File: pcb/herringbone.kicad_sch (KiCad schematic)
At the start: 93 parts, among them U1 ATmega328P-PU, Y1 16MHz

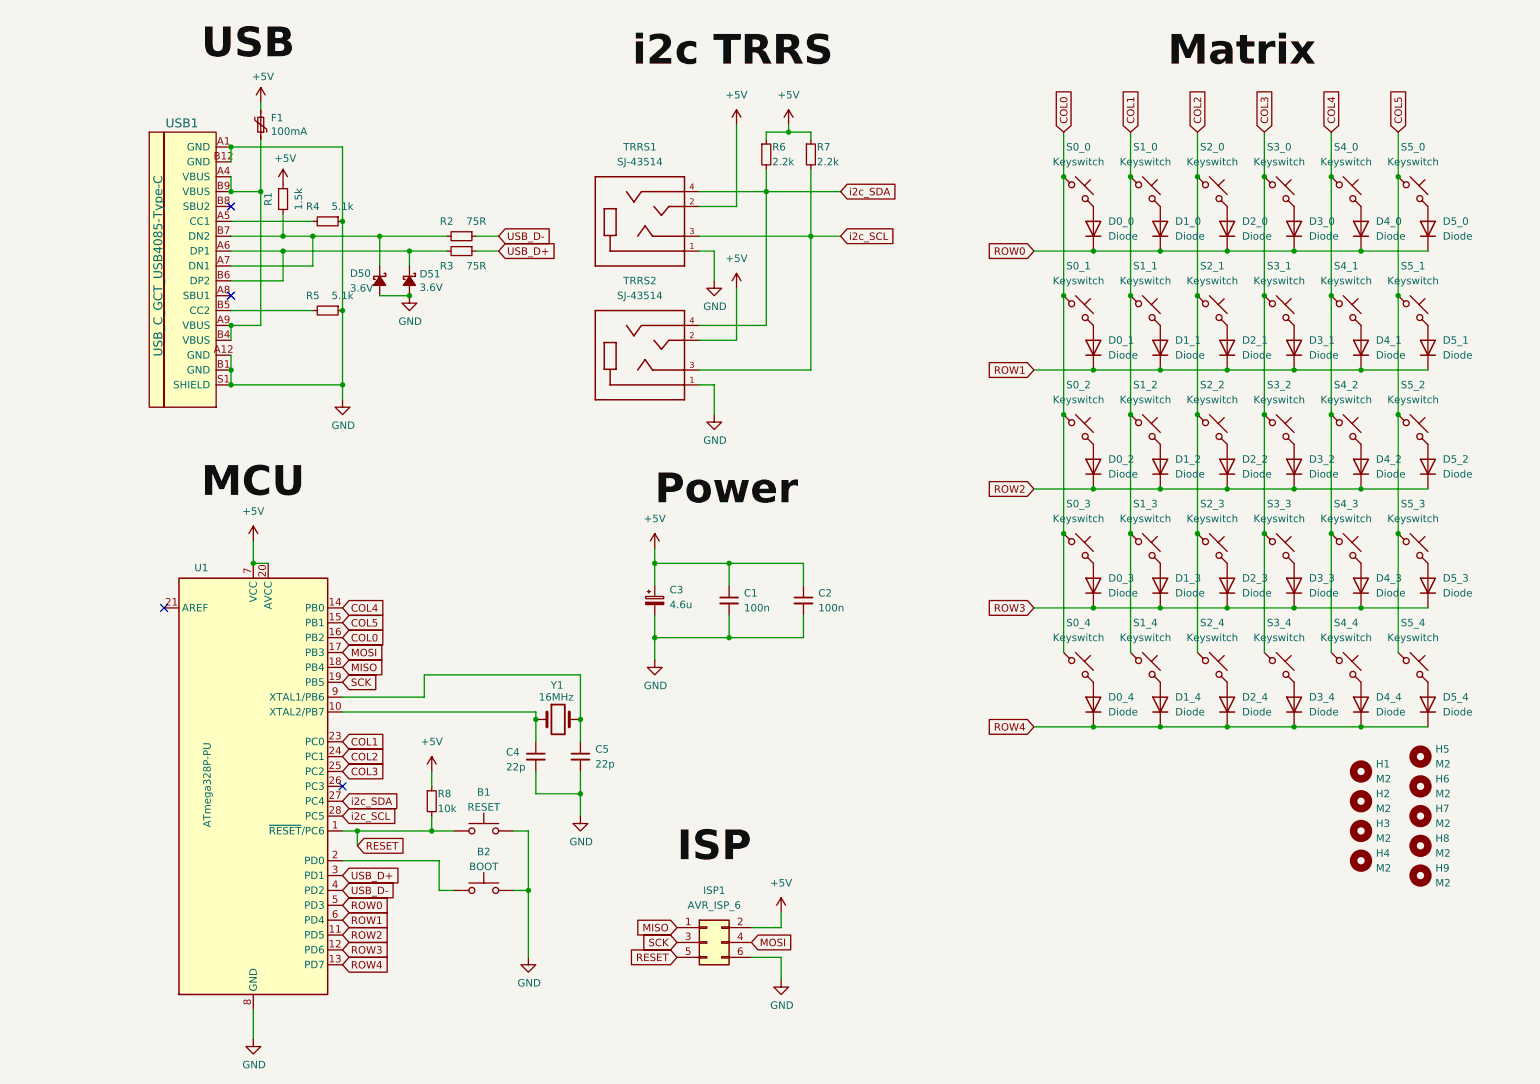
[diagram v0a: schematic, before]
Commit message: Move kicad projects to subfolders.
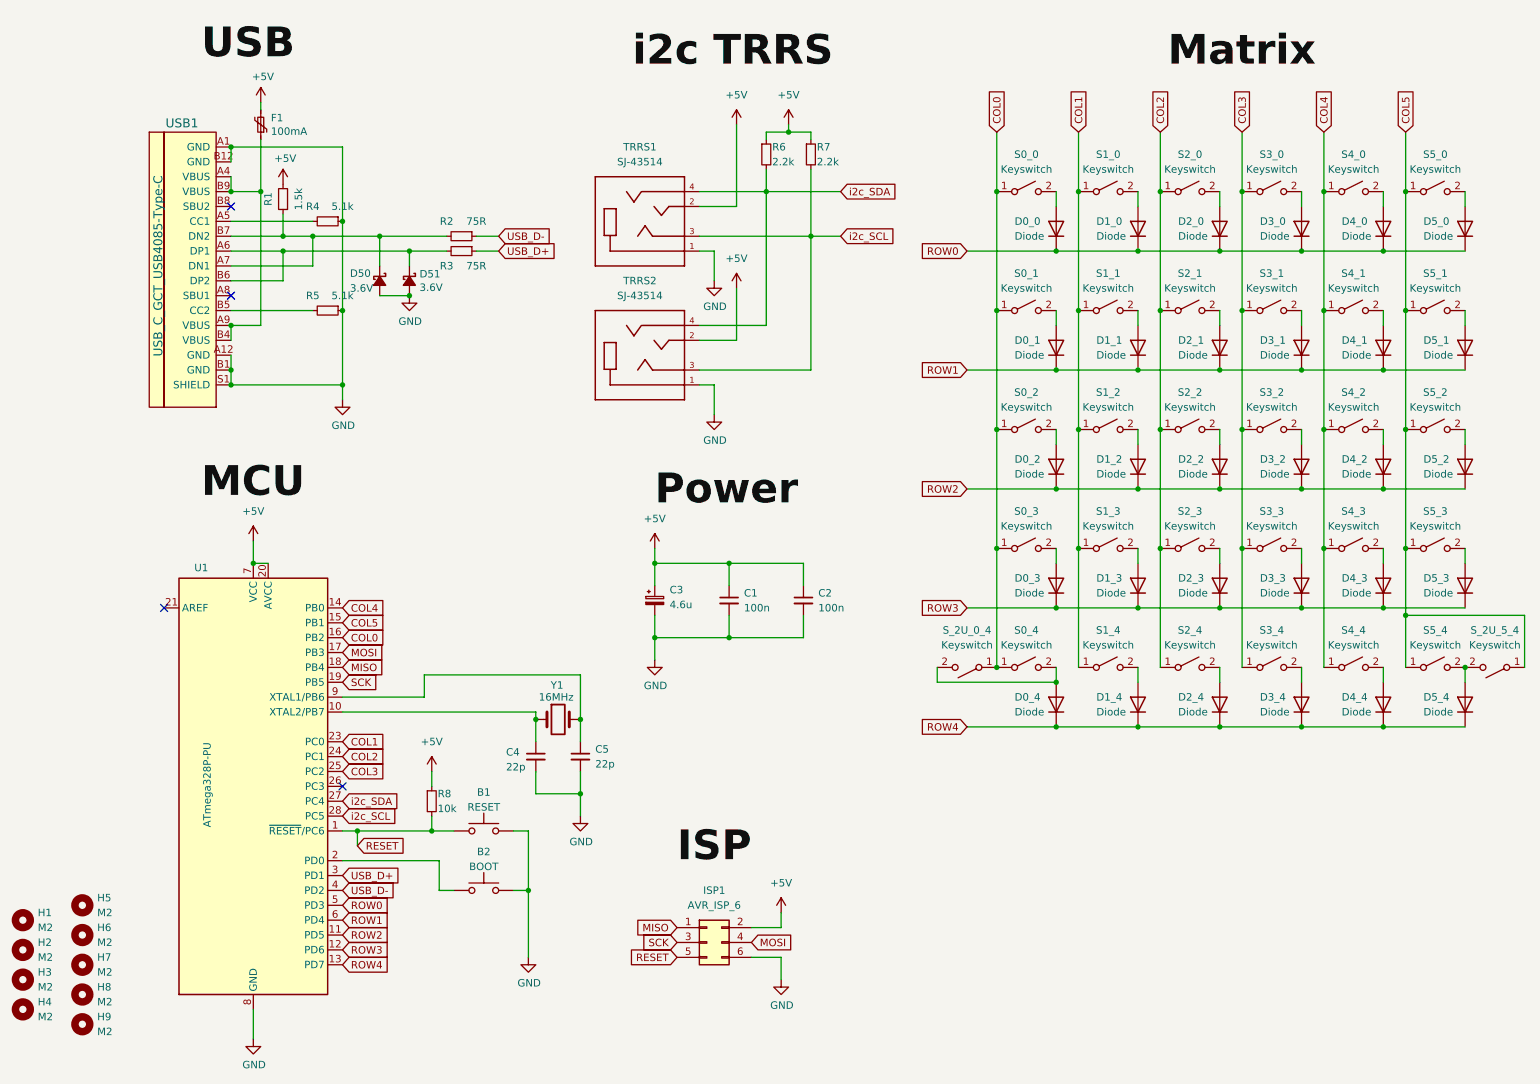
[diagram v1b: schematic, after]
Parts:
- added S_2U_0_4, S_2U_5_4: Keyswitch, PCM_Switch_Keyboard_Hotswap_Kailh:SW_Hotswap_Kailh_MX_2.00u, symbol Switch:SW_SPST
- D0_0, D0_1, D0_2, D0_3, D0_4, D1_0, D1_1, D1_2, D1_3, D1_4, D2_0, D2_1, D2_2, D2_3, D2_4, D3_0, D3_1, D3_2, D3_3, D3_4, D4_0, D4_1, D4_2, D4_3, D4_4, D5_0, D5_1, D5_2, D5_3, D5_4: symbol ScottoKeebs:Placeholder_Diode -> Device:D
- S0_0, S0_1, S0_2, S0_3, S0_4, S1_0, S1_1, S1_2, S1_3, S1_4, S2_0, S2_1, S2_2, S2_3, S2_4, S3_0, S3_1, S3_2, S3_3, S3_4, S4_0, S4_1, S4_2, S4_3, S4_4, S5_0, S5_1, S5_2, S5_3, S5_4: footprint ScottoKeebs_Hotswap:Hotswap_MX_1.00u -> PCM_Switch_Keyboard_Hotswap_Kailh:SW_Hotswap_Kailh_MX_1.00u; symbol ScottoKeebs:Placeholder_Keyswitch -> Switch:SW_SPST
- U1: footprint herringbone:DIP-28_W7.62mm_Socket -> herringbone:ATMEGA328-PU_DIP-28_W7.62mm_Socket
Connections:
- net COL0: now also S_2U_0_4.1 (A)
- net COL5: now also S_2U_5_4.1 (A)
- net at D5_4.2 (A), S5_4.2 (B): now also S_2U_5_4.2 (B)
- net at D0_4.2 (A), S0_4.2 (B): now also S_2U_0_4.2 (B)
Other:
- moved on the sheet: D0_0, D0_1, D0_2, D0_3, D0_4, D1_0, D1_1, D1_2, D1_3, D1_4, D2_0, D2_1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

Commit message: PCB rev2.
- Add LEDs
- Fix D+ D- USB pins for USBaspLoader to be happy
- Widen power Lines
- Allow for 2U keys in bottom corners
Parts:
- added L0, L1: LED, LED_THT:LED_D3.0mm, symbol Device:LED
- added R10, R9: 5.1k, herringbone:R_Axial_DIN0204_L3.6mm_D1.6mm_P5.08mm_Horizontal, symbol Device:R_Small
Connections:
- net GND: now also B2.1, R10.1, R9.1; no longer B2.2
- net ROW0: now also B2.2, U1.2 (PD0); no longer U1.5 (PD3)
- net USB_D+: now also U1.4 (PD2); no longer U1.3 (PD1)
- net USB_D-: now also U1.5 (PD3); no longer U1.4 (PD2)
- net LED0: now reaches U1.26 (PC3)
- net LED0: now also L0.2 (A)
- new net: L0.1 (K), R9.2
- new net: L1.1 (K), R10.2
- new net LED1: L1.2 (A), U1.3 (PD1)
- no-connect marks 4 -> 3
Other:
- moved on the sheet: B2
